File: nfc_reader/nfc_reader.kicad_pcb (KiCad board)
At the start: 2 copper layers, 54 x 85.7 mm, 79 parts, among them J1 USB_C, J2 Qwiic, J3 DEBUG, SW6 RESET, SW7 BOOT, U1 HX9193-33GB, U4 W25QXX128MBIT, U5 RP2040, Y1 12MHz, Y2 27.12MHz

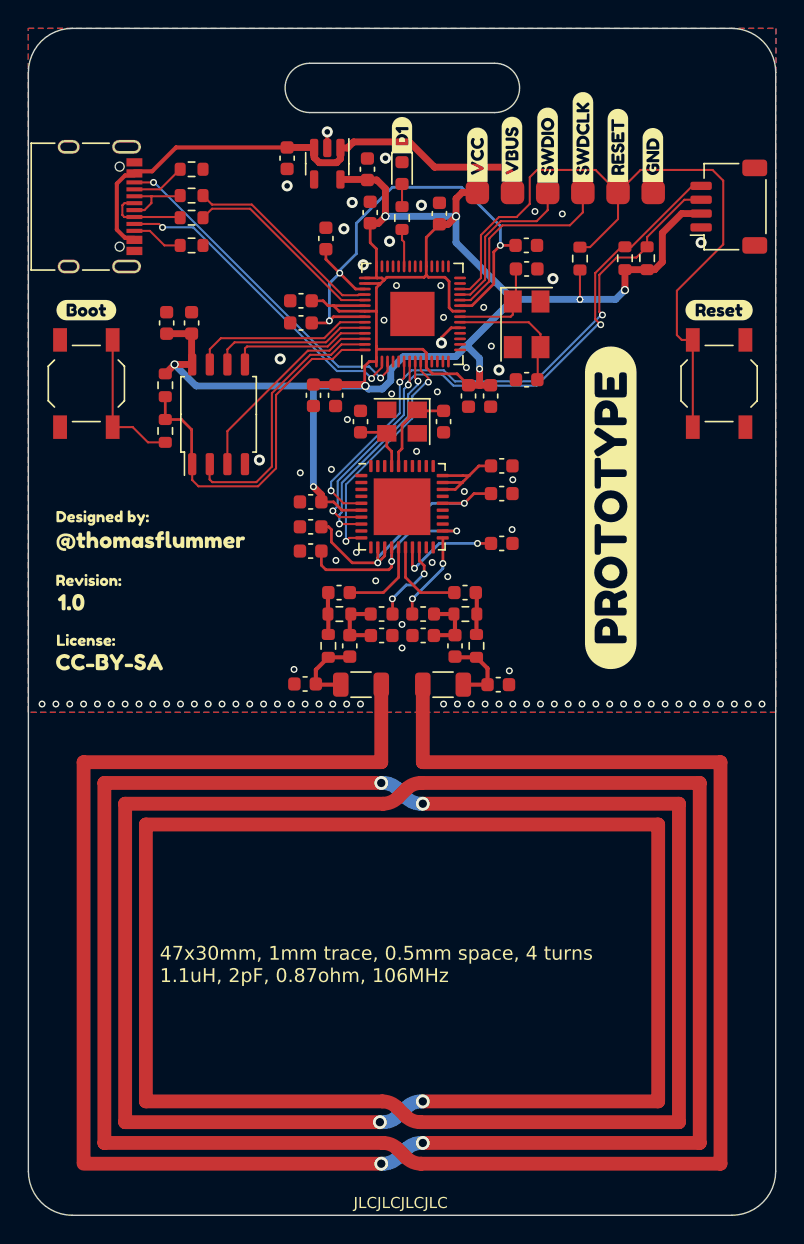
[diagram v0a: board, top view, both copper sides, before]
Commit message: Added front artwork to nfc_reader
Also
- Fixed error with missing power to PN7150 radio
- Added two buttons and two LEDs
- Moved things around a little
- Updated BOM and created pos file
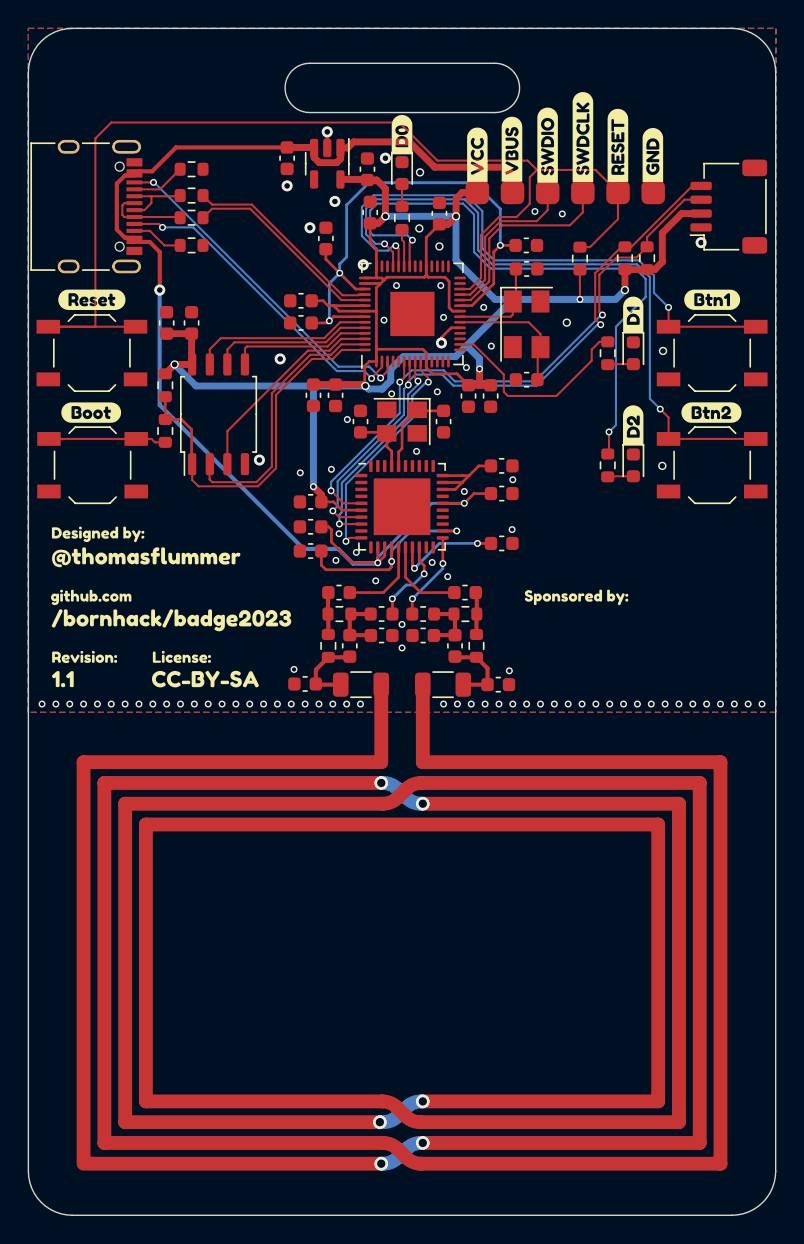
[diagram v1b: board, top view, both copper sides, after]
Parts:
- removed kibuzzard-6457AC4A: G***, kibuzzard-6457AC4A
- removed kibuzzard-645C0F6F: G***, kibuzzard-645C0F6F
- removed kibuzzard-645C1158: G***, kibuzzard-645C1158
- added D1: LED, LED_SMD:LED_0603_1608Metric, F.Cu at (99.6, 74.3)
- added D2: LED, LED_SMD:LED_0603_1608Metric, F.Cu at (99.6, 82.4)
- added R17: 1k, Resistor_SMD:R_0603_1608Metric, F.Cu at (97.7, 74.3)
- added R18: 1k, Resistor_SMD:R_0603_1608Metric, F.Cu at (97.7, 82.4)
- added SW1: TS5220A, Button_Switch_SMD:SW_SPST_TL3342, F.Cu at (105.3, 74.2)
- added SW2: TS5220A, Button_Switch_SMD:SW_SPST_TL3342, F.Cu at (105.3, 82.3)
- added kibuzzard-647C7A14: G***, kibuzzard-647C7A14, F.Cu at (58.4, 97.8)
- added kibuzzard-647C8669: G***, kibuzzard-647C8669, F.Cu at (82.9, 58.5)
- added kibuzzard-647C8670: G***, kibuzzard-647C8670, F.Cu at (99.6, 71.5)
- added kibuzzard-647C8676: G***, kibuzzard-647C8676, F.Cu at (99.6, 79.5)
- added kibuzzard-647C89AC: G***, kibuzzard-647C89AC, F.Cu at (105.3, 70.4)
- added kibuzzard-647C89B2: G***, kibuzzard-647C89B2, F.Cu at (105.2, 78.5)
- added kibuzzard-64945DE3: G***, kibuzzard-64945DE3, F.Cu at (60.4, 91.9)
- added kibuzzard-64945DF1: G***, kibuzzard-64945DF1, F.Cu at (66.2, 93.5)
- added kibuzzard-64946152: G***, kibuzzard-64946152, F.Cu at (95.5, 91.9)
- C27, C28: value 212.2pF/16V -> 200pF/16V, NP0, 5%
- C29, C30: value 206.3pF/50V -> 200pF/16V, NP0, 5%
- C31, C32: value 27.6pF/50V -> 27pF/50V, NP0, 2%
- J2: value Qwiic -> LCSC C145956
- L1, L2: value 560nH -> 560nH, 5%
- R15, R16: value 2.01R -> 2.00R 1%
- R3, R4: value 1K -> 1k
- SW6: value RESET -> TS5220A
- SW7: value BOOT -> TS5220A
- U3: value ~ -> PN7150B0HN/C11002Y
- Y1: value 12MHz -> 12MHz, 20pF
- Y2: value 27.12MHz -> 27.12MHz, 10pF
- moved SW6 45.4 mm to (60.5, 74.2), turned to 180 degrees
- moved kibuzzard-6457ABA7 45.3 mm to (60.5, 70.4)
- moved kibuzzard-6457AB78 7.41 mm to (60.4, 78.5)
- moved kibuzzard-645C118B 7.03 mm to (67.0, 96.2)
- moved kibuzzard-645C11AA 7.03 mm to (68.7, 97.8)
- moved SW7 5.92 mm to (60.5, 82.3), turned to 180 degrees
- moved kibuzzard-645C1150 5.56 mm to (59.9, 96.2)
- moved kibuzzard-645C104C 1.22 mm to (64.4, 89.0)
- moved kibuzzard-645C107E 1.22 mm to (60.9, 87.3)
- moved G*** 0.22 mm to (82.9, 93.6)
- renumbered D1 to D0
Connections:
- C1 pad 1: /rp2040/USB_VBUS -> /VUSB
- C19 pad 1: /PN7150 reader/VBAT -> /VUSB
- C21 pad 1: /PN7150 reader/VBAT -> /VUSB
- J1 pad A4: /rp2040/USB_VBUS -> /VUSB
- J1 pad A9: /rp2040/USB_VBUS -> /VUSB
- J1 pad B4: /rp2040/USB_VBUS -> /VUSB
- J1 pad B9: /rp2040/USB_VBUS -> /VUSB
- J3 pad 2: /rp2040/USB_VBUS -> /VUSB
- U1 pad 1: /rp2040/USB_VBUS -> /VUSB
- U1 pad 3: /rp2040/USB_VBUS -> /VUSB
- U3 pad 12: /PN7150 reader/VBAT -> /VUSB
- U3 pad 13: /PN7150 reader/VBAT -> /VUSB
- U3 pad 26: /PN7150 reader/VBAT -> /VUSB
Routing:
- net /VUSB: track 0.00 -> 92.4 mm, vias 0 -> 3
- net /rp2040/A1: track 0.00 -> 48.6 mm, vias 0 -> 2
- net /rp2040/PWM1/AUD_MCLK: track 0.00 -> 44.6 mm, vias 0 -> 2
- net /rp2040/A0: track 0.00 -> 42.6 mm, vias 0 -> 2
- net /rp2040/USB_VBUS: track 38.6 -> 0.00 mm
- net /rp2040/~{RESET}: track 52.8 -> 81.2 mm
- net /PN7150 reader/VBAT: track 20.2 -> 0.00 mm, vias 2 -> 0
- net /rp2040/PWM0: track 0.00 -> 15.0 mm
- net +1V1: track 37.5 -> 39.7 mm
- net /rp2040/~{BOOT}: track 10.6 -> 8.50 mm
- net Net-(D2-A): track 0.00 -> 1.81 mm
- net Net-(D1-A): track 0.00 -> 1.81 mm
- net VCC: track 142.4 -> 143.1 mm
- net GND: vias 90 -> 92
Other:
- board text removed: "47x30mm, 1mm trace, 0.5mm space, 4 turns 1.1uH, 2pF, 0.87ohm, 106MHz"
- board text removed: "JLCJLCJLCJLC"
